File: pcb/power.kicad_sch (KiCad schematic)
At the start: 1 part, among them J1 Screw_Terminal_01x02

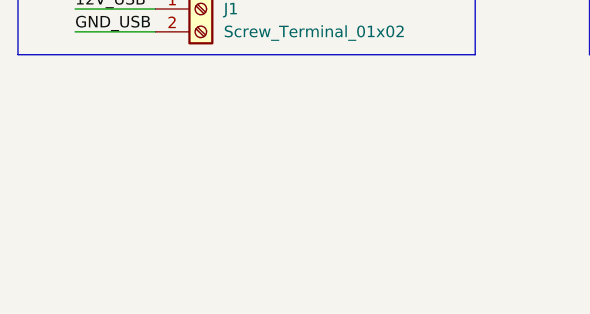
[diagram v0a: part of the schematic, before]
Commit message: Create STM32 project, expand ADC and GPIO schematic
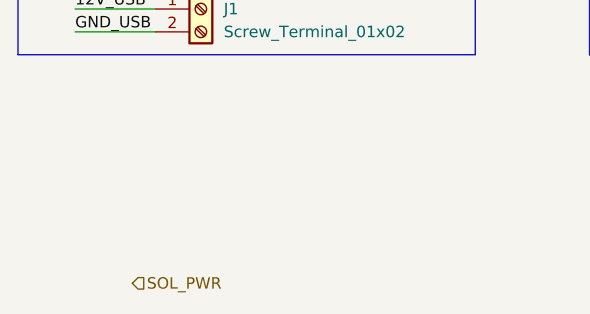
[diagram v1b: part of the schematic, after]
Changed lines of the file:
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@@
+		)
+	)
+	(hierarchical_label "SOL_PWR"
+		(shape input)
+		(at 114.3 101.6 0)
+		(effects
+			(font
+				(size 1.27 1.27)
+			)
+			(justify left)
 		)
 	)

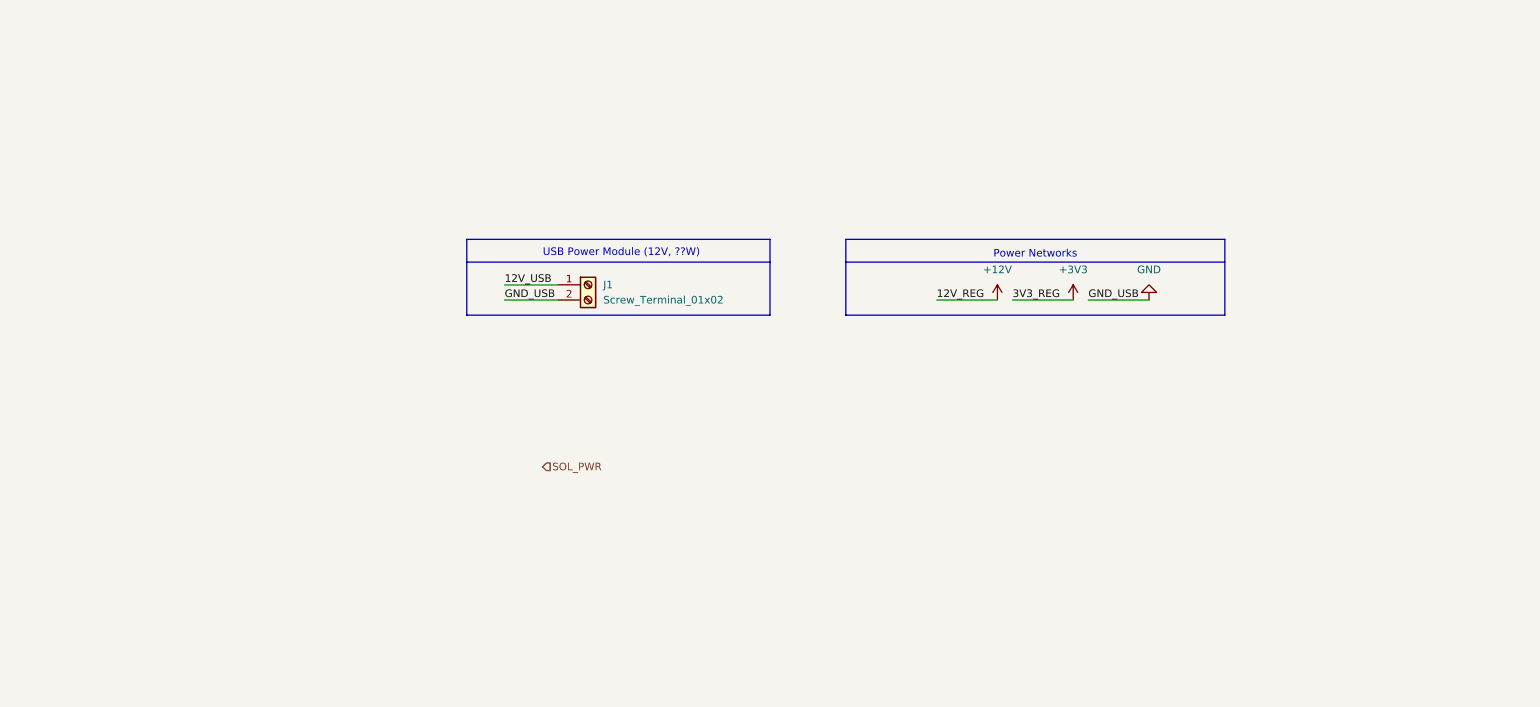
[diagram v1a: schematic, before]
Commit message: Main PCB nearly done, created resolver PCB, more STM32 work
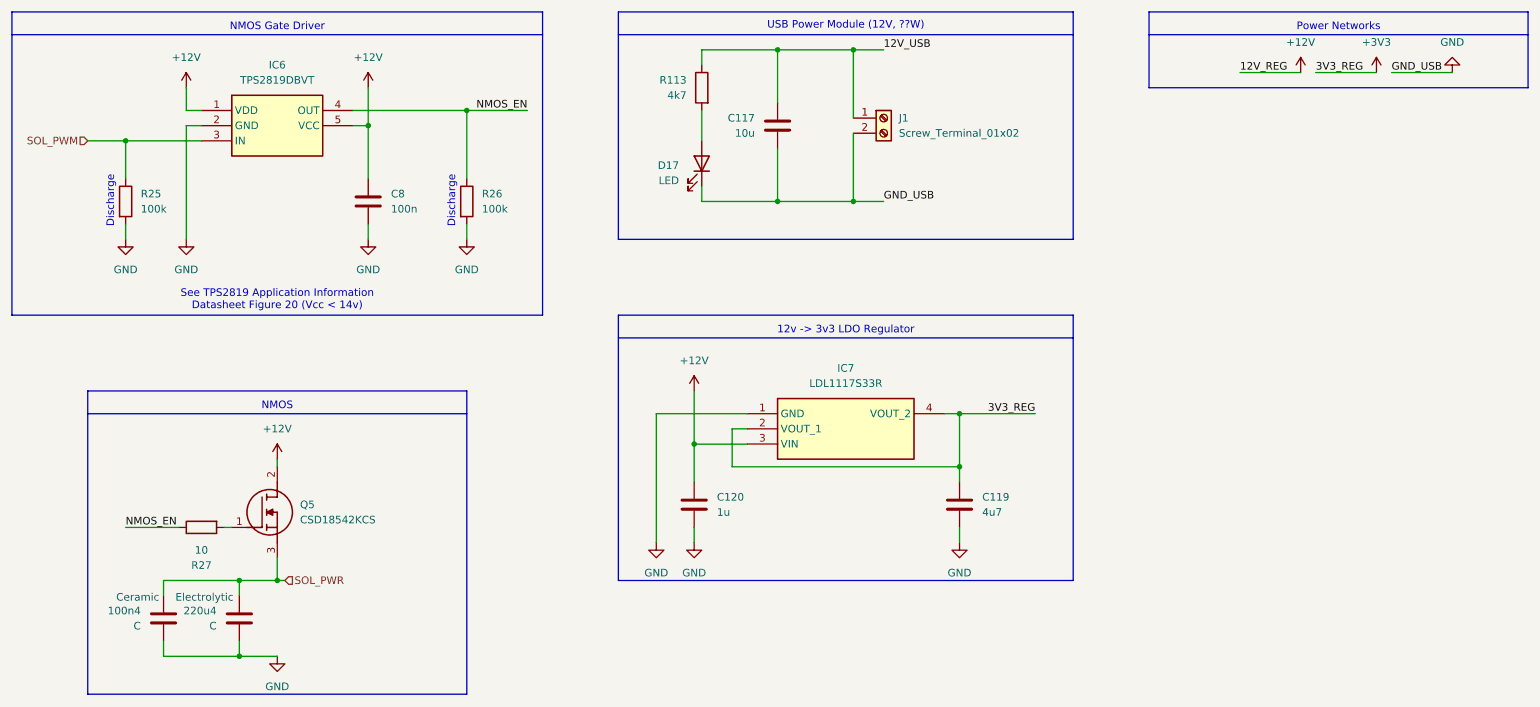
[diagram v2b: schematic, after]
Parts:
- added 100n4, 220u4: C, symbol Device:C
- added C117: 10u, Capacitor_SMD:C_0603_1608Metric, symbol Device:C
- added C119: 4u7, Capacitor_SMD:C_0805_2012Metric, symbol Device:C
- added C120: 1u, Capacitor_SMD:C_0805_2012Metric, symbol Device:C
- added C8: 100n, symbol Device:C
- added D17: LED, LED_SMD:LED_0603_1608Metric, symbol Device:LED
- added IC6: TPS2819DBVT, SOT95P280X145-5N, symbol TPS2819DBVT:TPS2819DBVT
- added IC7: LDL1117S33R, SOT230P700X180-4N, symbol LDL1117S33R:LDL1117S33R
- added Q5: CSD18542KCS, TO254P470X1016X2016-3P, symbol CSD18542KCS:CSD18542KCS
- added R113: 4k7, Resistor_SMD:R_0603_1608Metric, symbol Device:R
- added R25, R26: 100k, symbol Device:R
- added R27: 10, symbol Device:R
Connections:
- net +12V: now also C120.1, C8.1, IC6.1 (VDD), IC6.5 (VCC), IC7.3 (VIN), Q5.2 (D)
- net +3V3: now also C119.1, IC7.2 (VOUT_1), IC7.4 (VOUT_2)
- net 12V_USB: now also C117.1, R113.1
- net GND: now also 100n4.2, 220u4.2, C117.2, C119.2, C120.2, C8.2, D17.1 (K), IC6.2 (GND), IC7.1 (GND), R25.2, R26.2
- net SOL_PWR: now also 100n4.1, 220u4.1, Q5.3 (S)
- new net: Q5.1 (G), R27.2
- new net: D17.2 (A), R113.2
- new net NMOS_EN: IC6.4 (OUT), R26.1, R27.1
- new net SOL_PWM: IC6.3 (IN), R25.1
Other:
- note added: "12v -> 3v3 LDO Regulator"
- note added: "Discharge"
- note added: "NMOS"
- note added: "NMOS Gate Driver"
- note added: "See TPS2819 Application Information Datasheet Figure 20 (Vcc < 14v)"
- moved on the sheet: J1

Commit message: Completed all footprints
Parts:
- removed C8: 100n, symbol Device:C
- removed J1: Screw_Terminal_01x02, symbol Connector:Screw_Terminal_01x02
- added C109: 100n, Capacitor_SMD:C_0805_2012Metric, symbol Device:C
- added J15: TB005-762-02BE, footprints:TB005-762-02BE, symbol TB005-762-02BE:TB005-762-02BE
- 100n1: renamed from 100n4; value C -> C5; footprint (none) -> Capacitor_SMD:C_0805_2012Metric
- 220u1: renamed from 220u4; value C -> C4; footprint (none) -> Capacitor_SMD:CP_Elec_10x10
- C117: value 10u -> 220u; footprint Capacitor_SMD:C_0603_1608Metric -> Capacitor_SMD:C_0805_2012Metric
- D17: footprint LED_SMD:LED_0603_1608Metric -> Diode_SMD:D_0805_2012Metric
- IC6: footprint SOT95P280X145-5N -> footprints:SOT95P280X145-5N
- IC7: footprint SOT230P700X180-4N -> footprints:SOT230P700X180-4N
- Q5: footprint TO254P470X1016X2016-3P -> footprints:TO254P470X1016X2016-3P
- R113: footprint Resistor_SMD:R_0603_1608Metric -> Resistor_SMD:R_0805_2012Metric
- R25, R26, R27: footprint (none) -> Resistor_SMD:R_0805_2012Metric
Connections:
- net +12V: now also C109.1
- net 12V_USB: now also J15.1
- net GND: now also C109.2, J15.2

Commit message: PCB nearly done
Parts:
- C117: footprint Capacitor_SMD:C_0805_2012Metric -> Capacitor_SMD:CP_Elec_10x10
- C4: renamed from 220u1; value C4 -> 220u
- C5: renamed from 100n1; value C5 -> 100n

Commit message: PCB ready for review
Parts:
- removed Q5: CSD18542KCS, footprints:TO254P470X1016X2016-3P, symbol CSD18542KCS:CSD18542KCS
- added Q5: STH315N10F7-2, footprints:STH315N10F72, symbol STH315N10F7-2:STH315N10F7-2
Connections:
- net +12V: now also Q5.2 (D)
- net SOL_PWR: now also Q5.3 (S)
- net at R27.2: now also Q5.1 (G)

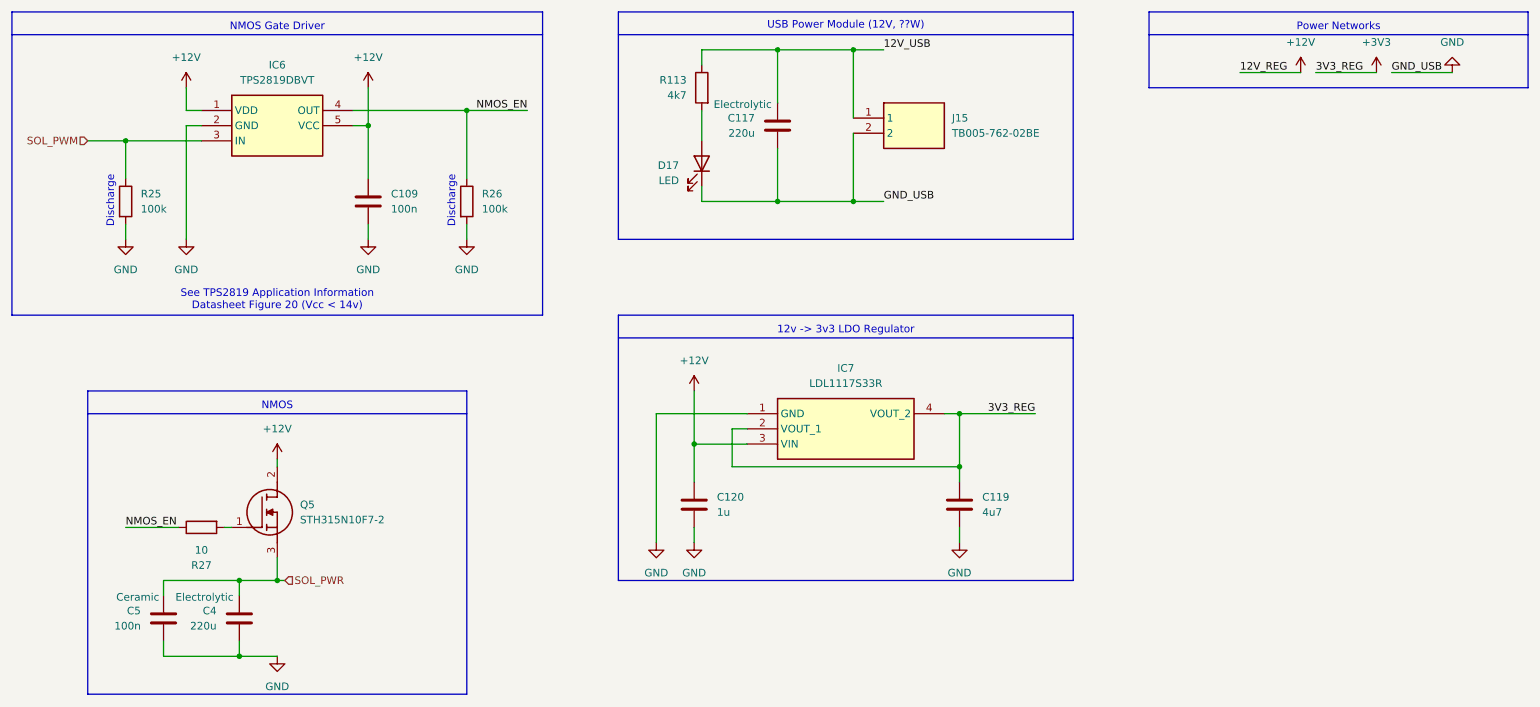
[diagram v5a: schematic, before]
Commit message: I forgot to put the holes in
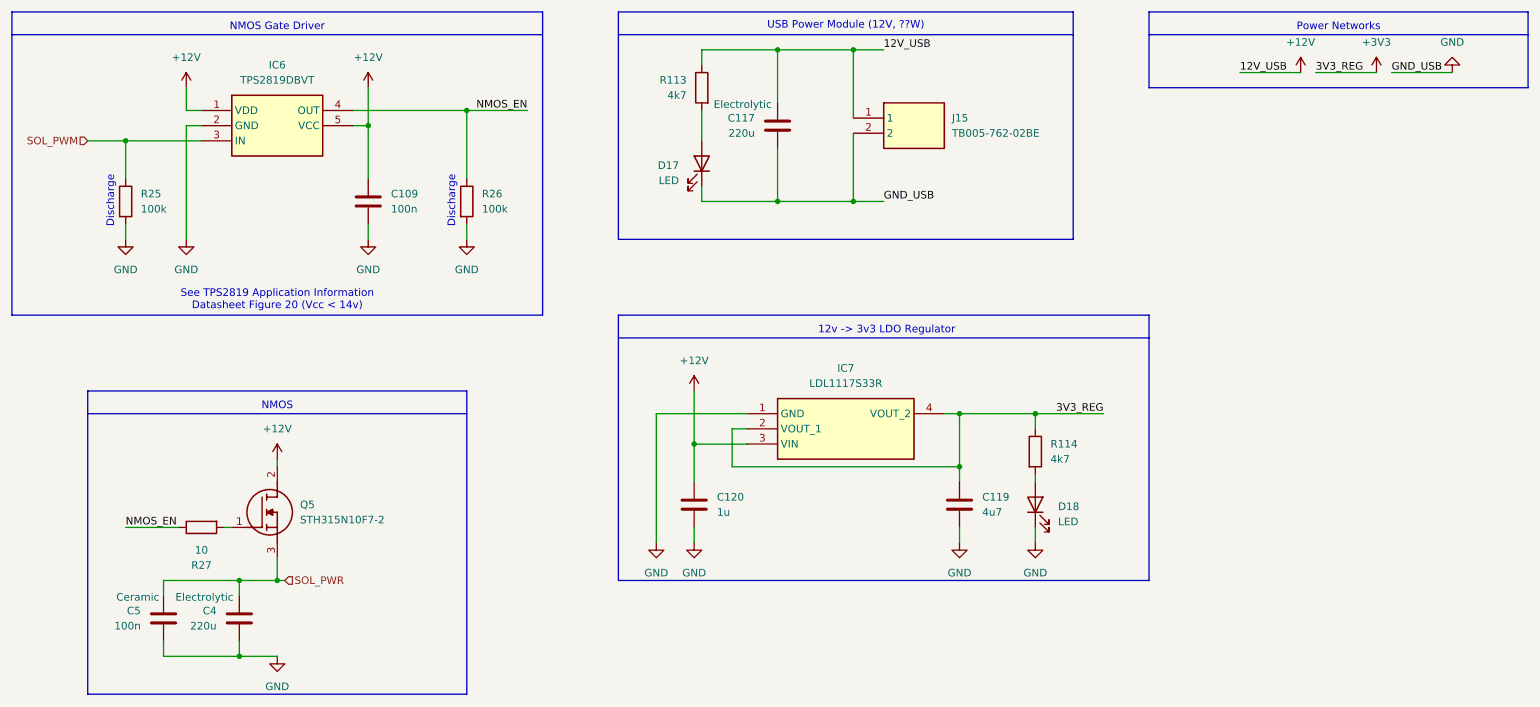
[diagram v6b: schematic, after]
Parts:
- added D18: LED, Diode_SMD:D_0805_2012Metric, symbol Device:LED
- added R114: 4k7, Resistor_SMD:R_0805_2012Metric, symbol Device:R
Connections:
- net 12V_USB is gone; now on net +12V: C117.1, J15.1, R113.1
- net +3V3: now also R114.1
- net GND: now also D18.1 (K)
- new net: D18.2 (A), R114.2
